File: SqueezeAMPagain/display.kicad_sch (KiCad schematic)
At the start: 0 parts

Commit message: Update .gitignore, L_Radial_D12.0mm_P5+6+7.00mm_Fastron_11P.kicad_mod, SqueezeAMPagain.kicad_pcb, and 13 more files
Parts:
- added J8: Conn_02x08_Odd_Even, Connector_IDC:IDC-Header_2x08_P2.54mm_Vertical, symbol Connector_Generic:Conn_02x08_Odd_Even
- added U6: TSOP21xx, OptoDevice:Vishay_MOLD-3Pin, symbol Interface_Optical:TSOP21xx
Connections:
- net CS: now also J8.7 (Pin_7)
- net D/C: now also J8.5 (Pin_5)
- net LED: now also J8.2 (Pin_2)
- net MISO: now also J8.4 (Pin_4)
- net MOSI: now also J8.1 (Pin_1)
- net RESET: now also J8.6 (Pin_6)
- net SCK: now also J8.3 (Pin_3)
- new net +3.3V: J8.10 (Pin_10), J8.9 (Pin_9), U6.2 (Vs)
- new net GND: J8.16 (Pin_16), J8.8 (Pin_8)
- new net IO1: J8.11 (Pin_11)
- new net IO2: J8.12 (Pin_12)
- new net IO3: J8.13 (Pin_13)
- new net IO4: J8.14 (Pin_14)
- new net ~{WAKE}: J8.15 (Pin_15)
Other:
- note added: "i2c?"
- title: (none) -> Frontpanel connector

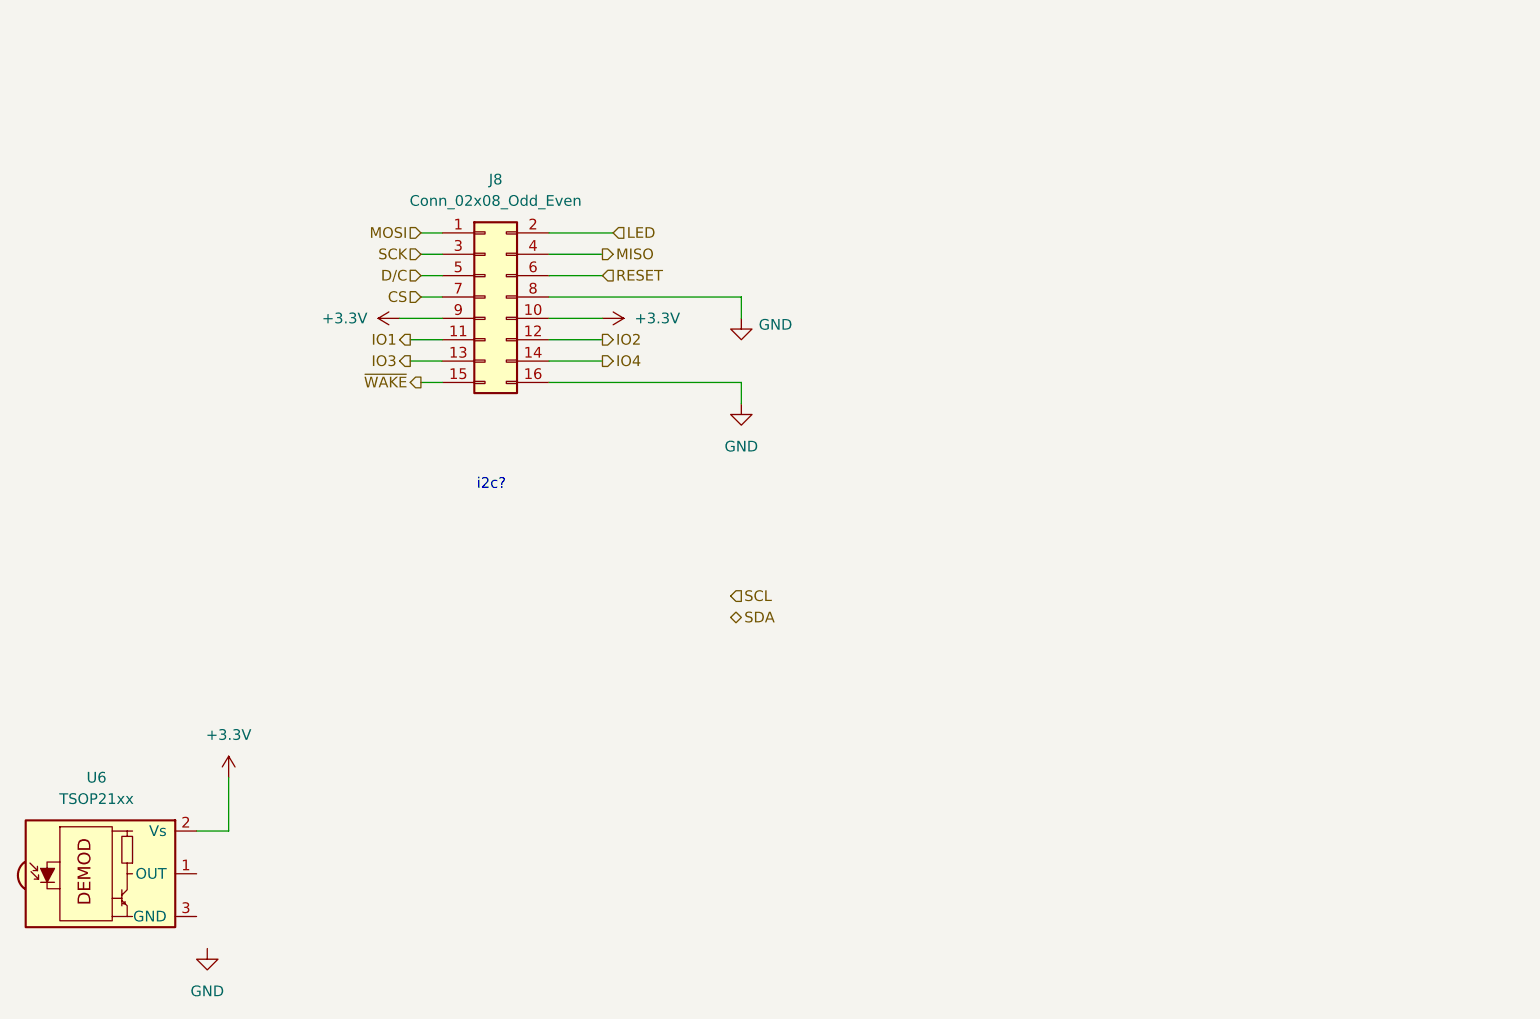
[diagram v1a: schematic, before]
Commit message: Update SqueezeAMPagain.kicad_pcb, SqueezeAMPagain.kicad_prl, SqueezeAMPagain.kicad_pro, and 5 more files
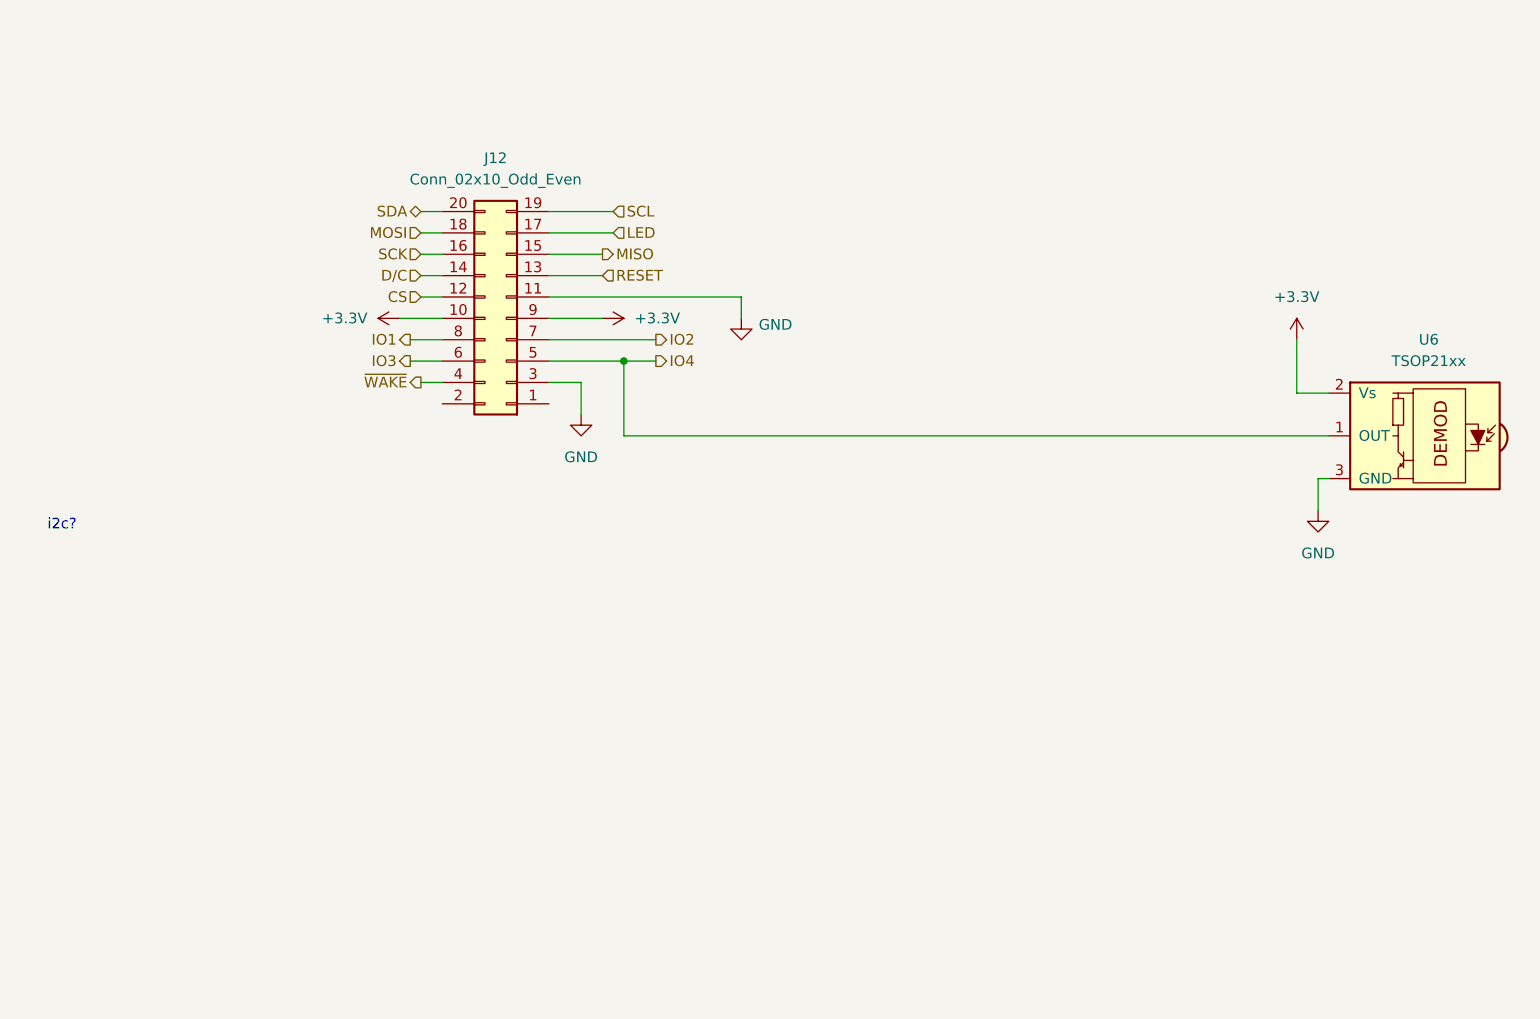
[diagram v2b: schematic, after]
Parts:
- removed J8: Conn_02x08_Odd_Even, Connector_IDC:IDC-Header_2x08_P2.54mm_Vertical, symbol Connector_Generic:Conn_02x08_Odd_Even
- added J12: Conn_02x10_Odd_Even, Connector_IDC:IDC-Header_2x10_P2.54mm_Horizontal, symbol Connector_Generic:Conn_02x10_Odd_Even
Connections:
- net +3.3V: now also J12.10 (Pin_10), J12.9 (Pin_9)
- net CS: now also J12.12 (Pin_12)
- net D/C: now also J12.14 (Pin_14)
- net GND: now also U6.3 (GND), J12.11 (Pin_11), J12.3 (Pin_3)
- net IO1: now also J12.8 (Pin_8)
- net IO2: now also J12.7 (Pin_7)
- net IO3: now also J12.6 (Pin_6)
- net IO4: now also U6.1 (OUT), J12.5 (Pin_5)
- net LED: now also J12.17 (Pin_17)
- net MISO: now also J12.15 (Pin_15)
- net MOSI: now also J12.18 (Pin_18)
- net RESET: now also J12.13 (Pin_13)
- net SCK: now also J12.16 (Pin_16)
- net SCL: now also J12.19 (Pin_19)
- net SDA: now also J12.20 (Pin_20)
- net ~{WAKE}: now also J12.4 (Pin_4)
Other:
- moved on the sheet: U6

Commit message: Update SqueezeAMPagain.kicad_pcb, SqueezeAMPagain.kicad_prl, SqueezeAMPagain.kicad_pro, and 11 more files
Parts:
- renumbered J12 to J5, U6 to U4
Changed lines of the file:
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@@
 		(on_board yes)
 		(dnp no)
-		(property "Reference" "#PWR086"
+		(property "Reference" "#PWR077"
 			(at 157.48 83.82 0)
 			(effects
@@
 			(project ""
 				(path "/3675160b-d9e5-490e-b506-2a7966e79ed0/ee00a6dc-f977-4055-96a4-c54a9ac88e93"
-					(reference "#PWR086")
+					(reference "#PWR077")
 					(unit 1)
 				)
@@
 		(dnp no)
 		(fields_autoplaced yes)
-		(property "Reference" "#PWR092"
+		(property "Reference" "#PWR078"
 			(at 223.52 83.82 0)
 			(effects
@@
 			(project "SqueezeAMPagain"
 				(path "/3675160b-d9e5-490e-b506-2a7966e79ed0/ee00a6dc-f977-4055-96a4-c54a9ac88e93"
-					(reference "#PWR092")
+					(reference "#PWR078")
 					(unit 1)
 				)
@@
 		(dnp no)
 		(fields_autoplaced yes)
-		(property "Reference" "#PWR035"
+		(property "Reference" "#PWR076"
 			(at 137.16 77.47 0)
 			(effects
@@
 			(project "SqueezeAMPagain"
 				(path "/3675160b-d9e5-490e-b506-2a7966e79ed0/ee00a6dc-f977-4055-96a4-c54a9ac88e93"
-					(reference "#PWR035")
+					(reference "#PWR076")
 					(unit 1)
 				)
@@
 		(dnp no)
 		(fields_autoplaced yes)
-		(property "Reference" "U6"
+		(property "Reference" "U4"
 			(at 239.225 80.01 0)
 			(effects
@@
 			(project ""
 				(path "/3675160b-d9e5-490e-b506-2a7966e79ed0/ee00a6dc-f977-4055-96a4-c54a9ac88e93"
-					(reference "U6")
+					(reference "U4")
 					(unit 1)
 				)
@@
 		(dnp no)
 		(fields_autoplaced yes)
-		(property "Reference" "#PWR087"
+		(property "Reference" "#PWR075"
 			(at 138.43 95.25 0)
 			(effects
@@
 			(project "SqueezeAMPagain"
 				(path "/3675160b-d9e5-490e-b506-2a7966e79ed0/ee00a6dc-f977-4055-96a4-c54a9ac88e93"
-					(reference "#PWR087")
+					(reference "#PWR075")
 					(unit 1)
 				)
@@
 		(dnp no)
 		(fields_autoplaced yes)
-		(property "Reference" "J12"
+		(property "Reference" "J5"
 			(at 128.27 58.42 0)
 			(effects
@@
 			(project ""
 				(path "/3675160b-d9e5-490e-b506-2a7966e79ed0/ee00a6dc-f977-4055-96a4-c54a9ac88e93"
-					(reference "J12")
+					(reference "J5")
 					(unit 1)
 				)
@@
 		(dnp no)
 		(fields_autoplaced yes)
-		(property "Reference" "#PWR085"
+		(property "Reference" "#PWR074"
 			(at 120.65 77.47 0)
 			(effects
@@
 			(project ""
 				(path "/3675160b-d9e5-490e-b506-2a7966e79ed0/ee00a6dc-f977-4055-96a4-c54a9ac88e93"
-					(reference "#PWR085")
+					(reference "#PWR074")
 					(unit 1)
 				)
@@
 		(dnp no)
 		(fields_autoplaced yes)
-		(property "Reference" "#PWR093"
+		(property "Reference" "#PWR079"
 			(at 226.06 106.68 0)
 			(effects
@@
 			(project "SqueezeAMPagain"
 				(path "/3675160b-d9e5-490e-b506-2a7966e79ed0/ee00a6dc-f977-4055-96a4-c54a9ac88e93"
-					(reference "#PWR093")
-					(unit 1)
-				)
+					(reference "#PWR079")
+					(unit 1)
+				)

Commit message: Update SqueezeAMPagain.kicad_pcb, SqueezeAMPagain.kicad_prl, SqueezeAMPagain.kicad_pro, and 11 more files
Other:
- note added: "Frontpanel connector"
- note added: "IR receiver option"
- note added: "WAKE pullup to VIN!"
- note removed: "i2c?"
- title: Frontpanel connector -> SqueezeAMP_{again}
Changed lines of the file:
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@@
 	(paper "A4")
 	(title_block
-		(title "Frontpanel connector")
+		(title "SqueezeAMP_{again}")
+		(date "2024-08-23")
+		(rev "1.0")
 	)
 	(junction
@@
 		)
 	)
-	(text "i2c?\n"
+	(text "IR receiver option"
 		(exclude_from_sim no)
-		(at 76.708 102.108 0)
+		(at 235.712 64.262 0)
 		(effects
 			(font
+				(size 1.27 1.27)
+			)
+		)
+	)
+	(text "WAKE pullup to VIN!"
+		(exclude_from_sim no)
+		(at 97.536 85.598 0)
+		(effects
+			(font
+				(size 1.27 1.27)
+			)
+			(href "#12")
+		)
+	)
+	(text "Frontpanel connector"
+		(exclude_from_sim no)
+		(at 128.524 43.18 0)
+		(effects
+			(font

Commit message: v2
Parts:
- added FB6, FB7: 600Ω@100MHz 500mA, Inductor_SMD:L_0805_2012Metric, symbol Device:FerriteBead_Small
- J4: renamed from J5; now not fitted
- U3: renamed from U4; now not fitted
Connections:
- net +3.3V: now also FB6.1, FB7.2; no longer J4.10 (Pin_10), J4.9 (Pin_9), U3.2 (Vs)
- net GND: now also J4.1 (Pin_1); no longer J4.3 (Pin_3)
- net IO1: now also J4.10 (Pin_10); no longer J4.8 (Pin_8)
- net IO3: now also J4.8 (Pin_8); no longer J4.6 (Pin_6)
- net at J4.2 (Pin_2): now also FB6.2
- new net: FB7.1, J4.9 (Pin_9), U3.2 (Vs)
- new net IO5: J4.3 (Pin_3)
- new net IO6: J4.6 (Pin_6)
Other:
- note removed: "WAKE pullup to VIN!"

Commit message: wip
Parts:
- added FB10: 600Ω@100MHz 500mA, Inductor_SMD:L_0805_2012Metric, symbol Device:FerriteBead_Small
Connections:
- net at FB6.2, J4.2 (Pin_2): now also FB10.2
- new net +5V: FB10.1
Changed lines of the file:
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@@
+	)
+	(junction
+		(at 111.76 87.63)
+		(diameter 0)
+		(color 0 0 0 0)
 	)
 	(junction
@@
 	(wire
 		(pts
+			(xy 111.76 102.87) (xy 111.76 87.63)
+		)
+		(stroke
+			(width 0)
+			(type default)
+		)
+	)
+	(wire
+		(pts
 			(xy 134.62 69.85) (xy 140.97 69.85)
 		)
@@
 	(wire
 		(pts
-			(xy 101.6 87.63) (xy 121.92 87.63)
+			(xy 101.6 87.63) (xy 111.76 87.63)
 		)
 		(stroke
@@
 	(wire
 		(pts
+			(xy 100.33 102.87) (xy 111.76 102.87)
+		)
+		(stroke
+			(width 0)
+			(type default)
+		)
+	)
+	(wire
+		(pts
 			(xy 167.64 86.36) (xy 167.64 77.47)
 		)
@@
 	(wire
 		(pts
+			(xy 111.76 87.63) (xy 121.92 87.63)
+		)
+		(stroke
+			(width 0)
+			(type default)
+		)
+	)
+	(wire
+		(pts
 			(xy 118.11 80.01) (xy 121.92 80.01)
 		)
@@
 		(pts
 			(xy 119.38 74.93) (xy 121.92 74.93)
+		)
+		(stroke
+			(width 0)
+			(type default)
+		)
+	)
+	(wire
+		(pts
+			(xy 88.9 102.87) (xy 95.25 102.87)
 		)
 		(stroke
@@
 					(unit 1)
 				)
+			)
+		)
+	)
+	(symbol
+		(lib_id "power:+5V")
+		(at 88.9 102.87 90)
+		(unit 1)
+		(exclude_from_sim no)
+		(in_bom yes)
+		(on_board yes)
+		(dnp no)
+		(fields_autoplaced yes)
+		(property "Reference" "#PWR110"
+			(at 92.71 102.87 0)
+			(effects
+				(font
+					(size 1.27 1.27)
+				)
+				(hide yes)
+			)
+		)
+		(property "Value" "+5V"
+			(at 85.09 102.8699 90)
+			(effects
+				(font
+					(size 1.27 1.27)
+				)
+				(justify left)
+			)
+		)
+		(property "Footprint" ""
+			(at 88.9 102.87 0)
+			(effects
+				(font
+					(size 1.27 1.27)
+				)
+				(hide yes)
+			)
+		)
+		(property "Datasheet" ""
+			(at 88.9 102.87 0)
+			(effects
+				(font
+					(size 1.27 1.27)
+				)
+				(hide yes)
+			)
+		)
+		(property "Description" "Power symbol creates a global label with name \"+5V\""
+			(at 88.9 102.87 0)
+			(effects
+				(font
+					(size 1.27 1.27)
+				)
+				(hide yes)
+			)
+		)
+		(pin "1"
+		)
+		(instances
+			(project ""
+				(path "/3675160b-d9e5-490e-b506-2a7966e79ed0/ee00a6dc-f977-4055-96a4-c54a9ac88e93"
+					(reference "#PWR110")
+					(unit 1)
+				)
+			)
+		)
+	)
+	(symbol
+		(lib_id "Device:FerriteBead_Small")
+		(at 97.79 102.87 90)
+		(unit 1)
+		(exclude_from_sim no)
+		(in_bom yes)
+		(on_board yes)
+		(dnp yes)
+		(property "Reference" "FB10"
+			(at 94.234 105.41 90)
+			(effects
+				(font
+					(size 1.27 1.27)
+				)
+			)
+		)
+		(property "Value" "600Ω@100MHz 500mA"
+			(at 87.63 108.204 90)
+			(effects
+				(font
+					(size 1.27 1.27)
+				)
+			)
+		)
+		(property "Footprint" "Inductor_SMD:L_0805_2012Metric"
+			(at 97.79 104.648 90)
+			(effects
+				(font
+					(size 1.27 1.27)
+				)
+				(hide yes)
+			)
+		)
+		(property "Datasheet" "~"
+			(at 97.79 102.87 0)
+			(effects
+				(font
+					(size 1.27 1.27)
+				)
+				(hide yes)
+			)
+		)
+		(property "Description" "Ferrite bead, small symbol"
+			(at 97.79 102.87 0)
+			(effects
+				(font
+					(size 1.27 1.27)
+				)
+				(hide yes)
+			)
+		)
+		(property "JLCPCB#" "C1017"
+			(at 97.79 102.87 0)
+			(effects
+				(font
+					(size 1.27 1.27)
+				)
+				(hide yes)
+			)
+		)
+		(pin "2"
+		)
+		(pin "1"
+		)
+		(instances
+			(project "SqueezeAMPagain"
+				(path "/3675160b-d9e5-490e-b506-2a7966e79ed0/ee00a6dc-f977-4055-96a4-c54a9ac88e93"
+					(reference "FB10")
+					(unit 1)
+				)
